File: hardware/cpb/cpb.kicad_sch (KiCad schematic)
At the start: 192 parts, among them J1 SW1, J10 RBFJUMP, J11 μSW2, J12 ADC15IN, J13 μSW3, J14 Conn_02x20_Odd_Even, J15 Conn_02x20_Odd_Even, J16 DAC1BUF, J17 DAC2BUF, J2 SW2, J3 SW3, J4 SW4, J5 ADC4IN, J6 PISW1, J7 ADC5IN, J8 ADC14IN, J9 μSW1, Q1 IRF7406, Q10 NPN, Q11 IRF7406, Q12 NPN, Q13 BSS138PS,115, Q14 BSS138PS,115, Q15 IRF7406, Q16 NPN, Q17 MBT2222ADW1T1, Q18 MBT2222ADW1T1, Q19 BSS138PS,115, Q2 IRF7406, Q20 BSS138PS,115, Q21 IRF7406, Q22 NPN, Q23 IRF7406, Q24 NPN, Q25 NPN, Q26 IRF7406, Q27 NPN, Q28 NPN, Q3 NPN, Q4 NPN, Q5 IRF7406, Q6 NPN, Q7 IRF7406, Q8 MBT2222ADW1T1, Q9 MBT2222ADW1T1, U1 KF33BDT, U2 AP63205WU, U3 SC16IS750xBS, U4 STM32L072R_B-Z_Tx, U5 TS912, U6 ADR420ARMZ, Y1 1.8432MHz

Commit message: cpb: add additional input/output channels
Adding more I/O to make the board more versatile.  While we're at
it, clean up schematic and make some early footprint/part number
assignments.  I like this board.
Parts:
- removed Q10, Q12, Q16, Q22, Q24, Q25, Q27, Q28, Q3, Q4, Q6: NPN, symbol Simulation_SPICE:NPN
- removed Q11, Q15, Q2, Q21, Q23, Q26, Q5, Q7: IRF7406, Package_SO:SOIC-8_3.9x4.9mm_P1.27mm, symbol Transistor_FET:IRF7404
- added D6: RED, LED_SMD:LED_0805_2012Metric, symbol Device:LED
- added Q11, Q2, Q5, Q7: IRF7306, Package_SO:SOIC-8_3.9x4.9mm_P1.27mm, symbol Transistor_FET:IRF7324
- added Q12, Q22, Q27, Q28, Q6: MBT2222ADW1T1, Package_TO_SOT_SMD:SOT-363_SC-70-6, symbol Transistor_BJT:MBT2222ADW1T1
- added Q4: PMBT2222A, Package_TO_SOT_SMD:SOT-23, symbol Transistor_BJT:PMBT2222A
- added R94: 1.5k, Resistor_SMD:R_0603_1608Metric, symbol Device:R
- C1, C11, C16, C17, C18, C19, C2, C20, C21, C22, C23, C24, C25, C26, C27, C28, C29, C3, C30, C31, C32, C33, C34, C35, C36, C4, C5, C6, C7, C8: footprint (none) -> Capacitor_SMD:C_0603_1608Metric
- C10, C12, C13, C14, C15, C9: LCSC C1589 -> (none); Manufacturer_Name Samsung Electro-Mechanics -> (none); Manufacturer_Part_Number CL10B103KB8NNNC -> (none)
- D1, D2, D3, D4, D5: value LED -> RED; footprint (none) -> LED_SMD:LED_0805_2012Metric; LCSC (none) -> C84256
- FB1: value FerriteBead -> BLM21BD272SN1L; footprint (none) -> Inductor_SMD:L_0805_2012Metric; LCSC (none) -> C85839
- H1, H2, H3, H4: DNI DNI -> (none)
- J14: DNI NP_JLC -> (none)
- L1: value 4.7u -> 4.7uH; footprint (none) -> Inductor_SMD:L_Vishay_IHLP-2020; LCSC (none) -> C844991
- Q1: LCSC (none) -> C3279781
- Q13, Q14, Q19, Q20: Flight BSS138PS,115 -> (none); Manufacturer_Part_Number BSS138PS,115 -> (none); Proto BSS138PS,115 -> (none)
- Q17, Q18, Q8, Q9: Flight MBT2222ADW1T1G -> (none); Manufacturer_Name onsemi -> (none); Manufacturer_Part_Number MBT2222ADW1T1G -> (none); Proto MBT2222ADW1T1G -> (none)
- R1, R10, R11, R12, R13, R14, R15, R16, R17, R18, R19, R2, R20, R21, R22, R23, R24, R25, R26, R27, R28, R29, R3, R30, R31, R32, R33, R34, R35, R36, R37, R38, R39, R4, R40, R41, R42, R43, R44, R45, R46, R47, R48, R49, R5, R50, R51, R52, R53, R54, R55, R56, R57, R58, R59, R6, R60, R61, R62, R63, R64, R65, R66, R67, R68, R69, R7, R70, R71, R72, R73, R74, R75, R76, R77, R78, R79, R8, R80, R81, R82, R83, R84, R85, R86, R87, R88, R89, R9, R90, R91, R92, R93: footprint (none) -> Resistor_SMD:R_0603_1608Metric
- U1: LCSC (none) -> C283274
- U2: LCSC (none) -> C2071056
- U3: LCSC (none) -> C2651891
- U4: LCSC (none) -> C915968
- U5: LCSC (none) -> C73655
- U6: LCSC (none) -> C208143
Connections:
- net +7.5V: now also Q11.1 (S1), Q11.3 (S2), Q2.1 (S1), Q2.3 (S2), Q5.1 (S1), Q5.3 (S2), Q7.1 (S1), Q7.3 (S2)
- net GND: now also D6.1 (K), Q12.1 (E1), Q12.4 (E2), Q22.1 (E1), Q22.4 (E2), Q27.1 (E1), Q27.4 (E2), Q28.1 (E1), Q28.4 (E2), Q4.2 (E), Q6.1 (E1), Q6.4 (E2)
- net MICRONRST: now also Q28.3 (C2)
- net PI3V3: now also R94.1
- net uSW1: now also U4.55 (PB3); no longer U4.42 (PA9)
- net uSW2: now also U4.56 (PB4); no longer U4.43 (PA10)
- net uSW3: now also U4.57 (PB5); no longer U4.44 (PA11)
- net at R22.2, R27.1: now also Q12.5 (B2)
- net at R23.2: now also Q12.3 (C2), Q5.4 (G2)
- net at R15.2, R19.1: now also Q12.2 (B1)
- net at J6.1 (Pin_1): now also Q7.7 (D1), Q7.8 (D1)
- net at R36.2, R39.1: now also Q22.2 (B1)
- net at R38.2: now also Q22.6 (C1), Q7.2 (G1)
- net at R18.2: now also Q12.6 (C1), Q5.2 (G1)
- net at R7.2: now also Q2.2 (G1), Q6.6 (C1)
- net at J1.1 (Pin_1): now also Q2.7 (D1), Q2.8 (D1)
- net at R71.2, R75.1: now also Q27.5 (B2)
- net at R4.2, R8.1: now also Q6.2 (B1)
- net at R3.2, R5.1: now also Q4.1 (B)
- net at R70.2, R76.1: now also Q28.5 (B2), Q28.6 (C1)
- net at J3.1 (Pin_1): now also Q5.7 (D1), Q5.8 (D1)
- net at R74.2: now also Q11.4 (G2), Q27.3 (C2)
- net at J9.1 (Pin_1): now also Q7.5 (D2), Q7.6 (D2)
- net at J13.1 (Pin_1): now also Q11.5 (D2), Q11.6 (D2)
- net at R56.2, R60.1: now also Q22.5 (B2)
- net at J4.1 (Pin_1): now also Q5.5 (D2), Q5.6 (D2)
- net at R10.2, R12.1: now also Q6.5 (B2)
- net at R11.2: now also Q2.4 (G2), Q6.3 (C2)
- net at R66.2: now also Q11.2 (G1), Q27.6 (C1)
- net at R64.2, R67.1: now also Q27.2 (B1)
- net at Q1.4 (G), R6.2: now also Q4.3 (C)
- net at R59.2: now also Q22.3 (C2), Q7.4 (G2)
- net at J15.12 (Pin_12), R72.2: now also Q28.2 (B1)
- net at J2.1 (Pin_1): now also Q2.5 (D2), Q2.6 (D2)
- net at J11.1 (Pin_1): now also Q11.7 (D1), Q11.8 (D1)
- net ADC4 renamed ADC6
- net ADC5 renamed ADC7
- new net: D6.2 (A), R94.2
- no-connect marks 45 -> 46
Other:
- note added: "Assuming 1.8Vf"
- note added: "Layout allows divider, control of impedance, LPF or AC coupling. All these inputs are also hooked to timer pins, so they can be used for capture or signal generation instead."
- note removed: "Layout allows divider, control of impedance, LPF or AC coupling."
- moved on the sheet: C12, C13, C14, C15, C28, C29, C32, C33, C34, C35, C36, FB1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

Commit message: cpb: add README, assign components, cleanup schematic
Lots of general cleanup and preparation to enter real assignment of
components and design review phase.
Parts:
- added Q3: PMBT2222A, Package_TO_SOT_SMD:SOT-23, symbol Transistor_BJT:PMBT2222A
- added R95: 10k, Resistor_SMD:R_0603_1608Metric, symbol Device:R
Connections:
- net +3.3V: now also R95.1
- net GND: now also Q3.2 (E)
- net MICRONRST: now also Q3.3 (C)
- net at U3.18 (GPIO5/~{DTR}): now also R9.2; no longer R9.1
- net GPIORST: now reaches U3.19 (GPIO6/~{CD})
- net GPIORST: now also Q3.1 (B), R95.2
- net PIFAILSAFE: now reaches U3.20 (GPIO7/~{RI})
- net PIFAILSAFE: now also J15.7 (Pin_7)
- net at D1.1 (K): now also R9.1; no longer R9.2
- no-connect marks 46 -> 44
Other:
- note added: "All resistors 1% tol! All capacitors on batt/7.5V rated >= 25V All capacitors on other rails rated at least 10V"
- note added: "Allow either pi or I2C-UART to hold microcontroller in reset. Ensure PI02W cannot hold down micro's reset when unpowered, but preserve sense of signal so existing software works."
- note added: "Connections to screws can be open, closed, resistive or capacitive."
- note added: "Per STMicro Recommendation"
- note added: "μController reset control"
- note removed: "All resistors 1% tol!"
- note removed: "Ensure PI02W cannot hold down micro's reset when unpowered."
- moved on the sheet: C1, C11, C12, C13, C14, C15, C6, C7, C8, D1, J12, J5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

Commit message: cpb: fix net name typos, assign footprints
Fix errors found by DRC.

Assign footprints so that it is possible to go to layout.

Select crystal for UART.
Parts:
- C10: value 22pF -> 15pF
- C9: value 33pF -> 22pF
- J10: footprint (none) -> Connector_PinHeader_2.54mm:PinHeader_1x02_P2.54mm_Horizontal
- J11, J12, J13, J2, J3, J4, J5, J6, J7, J8, J9: footprint (none) -> Connector_JST:JST_XH_B2B-XH-AM_1x02_P2.50mm_Vertical
- J15: footprint (none) -> Connector_PinHeader_2.54mm:PinHeader_2x20_P2.54mm_Vertical
- J16, J17: footprint (none) -> Connector_JST:JST_XH_B3B-XH-AM_1x03_P2.50mm_Vertical
- J77: renamed from J1; footprint (none) -> Connector_JST:JST_XH_B2B-XH-AM_1x02_P2.50mm_Vertical
- U5: footprint (none) -> Package_SO:SOIC-8_3.9x4.9mm_P1.27mm
- Y1: value 1.8432MHz -> 14.7456MHz; footprint (none) -> Crystal:Crystal_SMD_3225-4Pin_3.2x2.5mm; symbol Device:Crystal -> Device:Crystal_GND24_Small
- renumbered J14 to J1
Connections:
- net 3.3V is gone; now on net +3.3V: R13.1, R14.1, R16.1, R17.1, R24.1, R25.1, R34.1, R35.1, R40.1, R41.1, R49.1, R50.1
- net MICRORX is gone; now on net UCRX: J15.3 (Pin_3)
- net MICROTX is gone; now on net UCTX: J15.5 (Pin_5)
- net GND: now also Y1.2, Y1.4
- net at C10.1, U3.2 (XTAL1): now also Y1.3; no longer Y1.2
- no-connect marks 44 -> 60
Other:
- moved on the sheet: C27, R87, R88, U5B

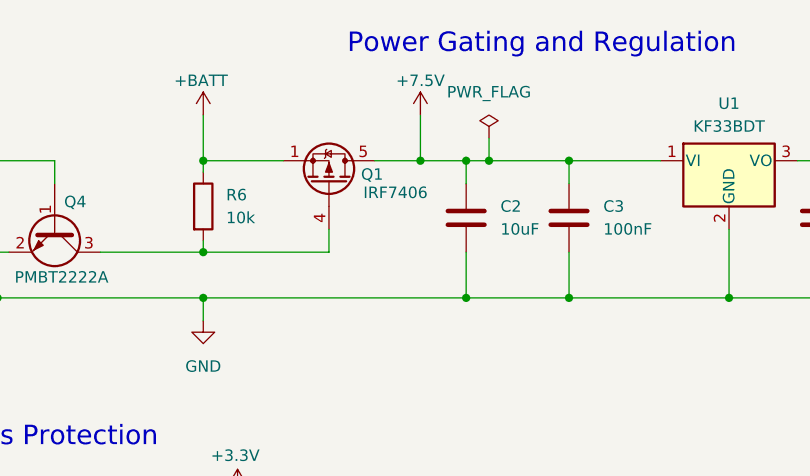
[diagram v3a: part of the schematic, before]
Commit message: cpb: substitute IRF9393 for IRF7406
IRF7406 availability is difficult right now, and IRF9393 seems to be
a strictly superior part.
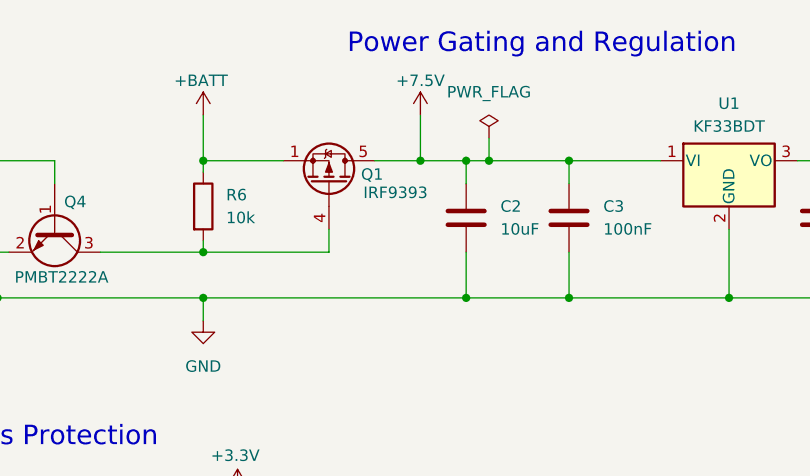
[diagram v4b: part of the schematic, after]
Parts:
- Q1: value IRF7406 -> IRF9393; LCSC C3279781 -> C520642
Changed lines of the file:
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@@
 			)
 		)
-		(property "Value" "IRF7406"
+		(property "Value" "IRF9393"
 			(at 88.9 32.766 90)
 			(effects
@@
 			)
 		)
-		(property "LCSC" "C3279781 "
+		(property "LCSC" "C520642"
 			(at 85.09 31.75 0)
 			(effects

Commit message: cpb: add octal H bridge, refactor to hierarchy
Big refactors here.

- Use hierarchical pages to represent duplicated circuits (e.g.
I2C protection, power switches).
- Add an octal H-bridge driver for magnetorquers
- Do some things for area reduction (resistor arrays)
- Attempt to name nets better and more consistently
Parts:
- removed C12, C13, C14, C15: 10nF, Capacitor_SMD:C_0603_1608Metric, symbol Device:C
- removed D1, D2: RED, LED_SMD:LED_0805_2012Metric, symbol Device:LED
- removed J2: SW2, Connector_JST:JST_XH_B2B-XH-AM_1x02_P2.50mm_Vertical, symbol Connector_Generic:Conn_01x02
- removed J3: SW3, Connector_JST:JST_XH_B2B-XH-AM_1x02_P2.50mm_Vertical, symbol Connector_Generic:Conn_01x02
- removed J4: SW4, Connector_JST:JST_XH_B2B-XH-AM_1x02_P2.50mm_Vertical, symbol Connector_Generic:Conn_01x02
- removed J5: ADC4IN, Connector_JST:JST_XH_B2B-XH-AM_1x02_P2.50mm_Vertical, symbol Connector_Generic:Conn_01x02
- removed J6: PISW1, Connector_JST:JST_XH_B2B-XH-AM_1x02_P2.50mm_Vertical, symbol Connector_Generic:Conn_01x02
- removed J7: ADC5IN, Connector_JST:JST_XH_B2B-XH-AM_1x02_P2.50mm_Vertical, symbol Connector_Generic:Conn_01x02
- removed J77: SW1, Connector_JST:JST_XH_B2B-XH-AM_1x02_P2.50mm_Vertical, symbol Connector_Generic:Conn_01x02
- removed J8: ADC14IN, Connector_JST:JST_XH_B2B-XH-AM_1x02_P2.50mm_Vertical, symbol Connector_Generic:Conn_01x02
- removed J9: μSW1, Connector_JST:JST_XH_B2B-XH-AM_1x02_P2.50mm_Vertical, symbol Connector_Generic:Conn_01x02
- removed Q11, Q2, Q5, Q7: IRF7306, Package_SO:SOIC-8_3.9x4.9mm_P1.27mm, symbol Transistor_FET:IRF7324
- removed Q12, Q17, Q18, Q22, Q27, Q6, Q8, Q9: MBT2222ADW1T1, Package_TO_SOT_SMD:SOT-363_SC-70-6, symbol Transistor_BJT:MBT2222ADW1T1
- removed Q13, Q14, Q19, Q20: BSS138PS,115, Package_TO_SOT_SMD:SOT-363_SC-70-6, symbol mainboard:BSS138DWQ-7
- removed Q3: PMBT2222A, Package_TO_SOT_SMD:SOT-23, symbol Transistor_BJT:PMBT2222A
- removed R1, R11, R13, R14, R16, R17, R18, R23, R34, R35, R38, R40, R41, R59, R6, R66, R7, R74, R95: 10k, Resistor_SMD:R_0603_1608Metric, symbol Device:R
- removed R10, R12, R15, R19, R22, R27, R3, R36, R39, R56, R60, R64, R67, R71, R75, R8: 4.7k, Resistor_SMD:R_0603_1608Metric, symbol Device:R
- removed R20, R21, R45, R46: 680, Resistor_SMD:R_0603_1608Metric, symbol Device:R
- removed R25, R49, R50: 100k, Resistor_SMD:R_0603_1608Metric, symbol Device:R
- removed R28, R29, R52, R53: 200k, Resistor_SMD:R_0603_1608Metric, symbol Device:R
- removed R32, R9, R94: 1.5k, Resistor_SMD:R_0603_1608Metric, symbol Device:R
- removed R68, R70, R72, R76: 3.3k, Resistor_SMD:R_0603_1608Metric, symbol Device:R
- added C3, C8: 22uF, Capacitor_SMD:C_0805_2012Metric, symbol Device:C
- added C5: 2.2uF, Capacitor_SMD:C_0603_1608Metric, symbol Device:C
- added D5: GPLED, LED_SMD:LED_0805_2012Metric, symbol Device:LED
- added D6: μCLED, LED_SMD:LED_0805_2012Metric, symbol Device:LED
- added D7: PILED, LED_SMD:LED_0805_2012Metric, symbol Device:LED
- added J10: SW1, Connector_JST:JST_PH_B2B-PH-K_1x02_P2.00mm_Vertical, symbol Connector_Generic:Conn_01x02
- added J14: μSW1, Connector_JST:JST_PH_B2B-PH-K_1x02_P2.00mm_Vertical, symbol Connector_Generic:Conn_01x02
- added J15: μSW2, Connector_JST:JST_PH_B2B-PH-K_1x02_P2.00mm_Vertical, symbol Connector_Generic:Conn_01x02
- added J16: μSW3, Connector_JST:JST_PH_B2B-PH-K_1x02_P2.00mm_Vertical, symbol Connector_Generic:Conn_01x02
- added J17: μSW4, Connector_JST:JST_PH_B2B-PH-K_1x02_P2.00mm_Vertical, symbol Connector_Generic:Conn_01x02
- added J2: I2CExt, Connector_JST:JST_PH_B5B-PH-K_1x05_P2.00mm_Vertical, symbol Connector_Generic:Conn_01x05
- added J7: ADC6/7, Connector_JST:JST_PH_B4B-PH-K_1x04_P2.00mm_Vertical, symbol Connector_Generic:Conn_01x04
- added J8: ADC2/3, Connector_JST:JST_PH_B4B-PH-K_1x04_P2.00mm_Vertical, symbol Connector_Generic:Conn_01x04
- added J9: 4FBRG, Connector_JST:JST_PHD_B8B-PHDSS_2x04_P2.00mm_Vertical, symbol Connector_Generic:Conn_01x08
- added Q4: PMBT2222A, Package_TO_SOT_SMD:SOT-23, symbol Transistor_BJT:PMBT2222A
- added R51: 10k, Resistor_SMD:R_0603_1608Metric, symbol Device:R
- added RN11: 3.3k, Resistor_SMD:R_Array_Convex_4x0603, symbol Device:R_Pack04_Split
- added RN12: 4.7k, Resistor_SMD:R_Array_Convex_4x0603, symbol Device:R_Pack04_Split
- added RN13: 1.5k, Resistor_SMD:R_Array_Convex_4x0603, symbol Device:R_Pack04_Split
- C10: renamed from C2; value 10uF -> 2.2uF
- D1: renamed from D3; value RED -> 7V5
- D2: renamed from D4; value RED -> 5V
- D3: renamed from D5; value RED -> 3V3
- D4: renamed from D6; value RED -> PI3V3
- J11: value μSW2 -> SW2; footprint Connector_JST:JST_XH_B2B-XH-AM_1x02_P2.50mm_Vertical -> Connector_JST:JST_PH_B2B-PH-K_1x02_P2.00mm_Vertical
- J12: value ADC15IN -> SW3; footprint Connector_JST:JST_XH_B2B-XH-AM_1x02_P2.50mm_Vertical -> Connector_JST:JST_PH_B2B-PH-K_1x02_P2.00mm_Vertical
- J13: value μSW3 -> PISW1; footprint Connector_JST:JST_XH_B2B-XH-AM_1x02_P2.50mm_Vertical -> Connector_JST:JST_PH_B2B-PH-K_1x02_P2.00mm_Vertical
- J3: renamed from J16; footprint Connector_JST:JST_XH_B3B-XH-AM_1x03_P2.50mm_Vertical -> Connector_JST:JST_PH_B3B-PH-K_1x03_P2.00mm_Vertical
- J4: renamed from J17; footprint Connector_JST:JST_XH_B3B-XH-AM_1x03_P2.50mm_Vertical -> Connector_JST:JST_PH_B3B-PH-K_1x03_P2.00mm_Vertical
- R24: value 100k -> 33
- R4: value 4.7k -> 200m 1W; footprint Resistor_SMD:R_0603_1608Metric -> Resistor_SMD:R_1206_3216Metric
- renumbered C20 to C1, C16 to C11, C23 to C12, C33 to C13, C3 to C14, C34 to C15, C35 to C16, C18 to C17, C24 to C18, C36 to C19, C21 to C2, C4 to C20, C5 to C21, C11 to C22, C30 to C23, C31 to C24, C17 to C26, C26 to C27, C6 to C28, C1 to C29, C28 to C30, C7 to C31, C29 to C32, C8 to C33, C9 to C34, C10 to C35, C22 to C4, C19 to C6, C27 to C7, C32 to C9, J15 to J1, J1 to J5, J10 to J99, Q4 to Q1, Q1 to Q2, Q28 to Q3, R84 to R10, R88 to R11, R77 to R12, R81 to R13, R83 to R14, R85 to R15, R89 to R16, R90 to R17, R62 to R18, R78 to R19, R86 to R20, R61 to R21, R43 to R22, R44 to R23, R91 to R25, R92 to R26, R26 to R27, R31 to R28, R33 to R29, R42 to R30, R93 to R31, R30 to R32, R37 to R33, R2 to R34, R82 to R37, R48 to R38, R58 to R39, R63 to R40, R69 to R41, R55 to R44, R65 to R45, R47 to R52, R51 to R53, R57 to R55, R79 to R6, R87 to R7, R73 to R8, R80 to R9, U5 to U1, U6 to U2, U1 to U3, U2 to U5, U3 to U6
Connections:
- net +3.3V: now also J2.2 (Pin_2), R51.1, RN11.5 (R4.2); no longer R24.1
- net +7.5V: now also C8.1, J2.3 (Pin_3)
- net +BATT: now also R4.1, C3.2, RN12.6 (R3.2); no longer Q2.1 (S), Q2.2 (S), Q2.3 (S)
- net ADC14: no longer R38.2, R39.1, R44.1
- net ADC15: no longer R40.2, R41.1, R45.1
- net ADC6: no longer U4.22 (PA6)
- net ADC7: no longer U4.23 (PA7)
- net GND: now also J11.1 (Pin_1), J13.1 (Pin_1), C3.1, C5.2, C8.2, D5.1 (K), D6.1 (K), D7.1 (K), J10.1 (Pin_1), J14.1 (Pin_1), J15.2 (Pin_2), J16.2 (Pin_2), J17.2 (Pin_2), J2.1 (Pin_1), J7.1 (Pin_1), J7.3 (Pin_3), J8.1 (Pin_1), J8.3 (Pin_3), Q4.2 (E), RN11.6 (R3.2), RN12.2 (R2.1); no longer J11.2 (Pin_2), J13.2 (Pin_2)
- net PI3V3: now also RN11.7 (R2.2), RN11.8 (R1.2), RN13.8 (R1.2)
- net REF2V: now also R24.2
- net SW1: no longer R4.1
- net UCRX: no longer R23.1, U4.59 (PB7)
- net UCTX: no longer R22.1, U4.58 (PB6)
- net at R32.2: now also J7.4 (Pin_4)
- net at R45.2: now also J8.2 (Pin_2); no longer J12.1 (Pin_1)
- net ADC2: now reaches U4.16 (PA2)
- net ADC2: now also R38.2, R39.1, R44.1
- net ADC3: now reaches U4.17 (PA3)
- net ADC3: now also R40.2, R41.1, R45.1
- net uSW4: now reaches U4.34 (PB13)
- net TIM3_CH2: now reaches U4.38 (PC7)
- net TIM3_CH2: now also RN13.6 (R3.2)
- net GPLED: now reaches U6.18 (GPIO5/~{DTR})
- net GPLED: now also RN13.7 (R2.2)
- net at R4.2: now also Q2.1 (S), Q2.2 (S), Q2.3 (S)
- net at Q1.1 (B): now also RN12.7 (R2.2), RN12.8 (R1.2); no longer R5.1
- net at D4.2 (A): now also RN13.1 (R1.1)
- net ~{RSTREQPI}: now reaches J1.12 (Pin_12), Q3.2 (B1)
- net ~{RSTREQPI}: now also RN11.1 (R1.1)
- net at Q3.5 (B2), Q3.6 (C1): now also RN11.2 (R2.1), RN11.3 (R3.1)
- net at R44.2: now also J8.4 (Pin_4)
- net at Q2.4 (G): now also C5.1, RN12.5 (R4.2); no longer Q1.3 (C)
- net at R33.2: now also J7.2 (Pin_2)
- net FBRGPWREN: now reaches J5.23 (Pin_23)
- net PILED: now reaches J1.33 (Pin_33)
- net PILED: now also RN13.5 (R4.2)
- net EN5V# renamed EN5V
- net EN5V: now also R5.1
- net GPIORST renamed RSTREQGPIO
- net RSTREQGPIO: now also Q4.1 (B), R51.2
- net MICRONRST renamed ~{MICRORST}
- net ~{MICRORST}: now also Q4.3 (C), RN11.4 (R4.1)
- net PICTS# renamed nPICTS
- net nPICTS: no longer J1.36 (Pin_36)
- net PIRTS# renamed nPIRTS
- net nPIRTS: no longer J1.11 (Pin_11)
- net PWRGATE renamed PRIPWREN
- net PRIPWREN: now also RN12.1 (R1.1)
- net RBF# renamed ~{RBF}
- net SCLMICRO renamed uSCL
- net SDAMICRO renamed uSDA
- new net: R24.1, U4.22 (PA6)
- new net: Q1.3 (C), RN12.3 (R3.1), RN12.4 (R4.1)
- new net: D5.2 (A), RN13.2 (R2.1)
- new net: D6.2 (A), RN13.3 (R3.1)
- new net: D7.2 (A), RN13.4 (R4.1)
- new net FourFullBridges/OUT1A: J9.1 (Pin_1)
- new net FourFullBridges/OUT1B: J9.2 (Pin_2)
- new net FourFullBridges/OUT2A: J9.3 (Pin_3)
- new net FourFullBridges/OUT2B: J9.4 (Pin_4)
- new net FourFullBridges/OUT3A: J9.5 (Pin_5)
- new net FourFullBridges/OUT3B: J9.6 (Pin_6)
- new net FourFullBridges/OUT4A: J9.7 (Pin_7)
- new net FourFullBridges/OUT4B: J9.8 (Pin_8)
- new net PairPowerSwitches1/OUT1: J10.2 (Pin_2)
- new net PairPowerSwitches1/OUT2: J11.2 (Pin_2)
- new net PairPowerSwitches2/OUT1: J12.1 (Pin_1)
- new net PairPowerSwitches2/OUT2: J13.2 (Pin_2)
- new net PairPowerSwitches3/OUT1: J14.2 (Pin_2)
- new net PairPowerSwitches3/OUT2: J15.1 (Pin_1)
- new net PairPowerSwitches4/OUT1: J16.1 (Pin_1)
- new net PairPowerSwitches4/OUT2: J17.1 (Pin_1)
- new net SCLEXT: J2.4 (Pin_4)
- new net SDAEXT: J2.5 (Pin_5)
- new net uRX: R23.1, U4.59 (PB7)
- new net uTX: R22.1, U4.58 (PB6)
- new net ~{PICTS}: J1.36 (Pin_36)
- new net ~{PIRTS}: J1.11 (Pin_11)
- no-connect marks 60 -> 55
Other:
- added sheet FourFullBridges (FourFullBridges.kicad_sch)
- added sheet I2CProtectionExt (I2CProtection.kicad_sch)
- added sheet I2CProtectionMicro (I2CProtection.kicad_sch)
- added sheet I2CProtectionUART (I2CProtection.kicad_sch)
- added sheet PairPowerSwitches1 (PairPowerSwitches.kicad_sch)
- added sheet PairPowerSwitches2 (PairPowerSwitches.kicad_sch)
- added sheet PairPowerSwitches3 (PairPowerSwitches.kicad_sch)
- added sheet PairPowerSwitches4 (PairPowerSwitches.kicad_sch)
- note added: "Address: 1001 000X (0x90 or 0x48)"
- note added: "Allow either pi or I2C-UART to hold microcontroller in reset. Ensure PI02W cannot hold down micro's reset when unpowered, but preserve sense of signal so existing programming software works."
- note added: "Also EVENTOUT, TIM3_CH1, or TIM22_CH1"
- note added: "Also EVENTOUT, TIM3_CH2, or TIM22_CH2"
- note added: "Also TIM2_CH3, TIM21_CH1, or UART TX Or comparator input."
- note added: "Also TIM2_CH4, TIM21_CH2, or UART RX; Or comparator input."
- note added: "Bulk Power Switches for Payloads"
- note added: "Decouple stack 3V3 even though we don't use it."
- note added: "Full Bridge for Magnetorquers"
- note added: "Layout allows divider, control of impedance, LPF or AC coupling. These pins have alternate functions (like timers for signal gen)."
- note added: "Linearize power switch to limit inrush; limit fault currents."
- note added: "PB6/PB7 are also an I2C SCL/SDA."
- note added: "Power is switched separately from everything else, for flexibility and robustness."
- note added: "Rail expected between 7.4 and 8.5V"
- note added: "Status LEDs"
- note added: "Threshold ~3A/V; dv/dt through thresh 909uV/us dA/dt 2.7mA/us XXX recalc 370us to reach an ampere; capacitors reach 7.5V in this time"
- note removed: "All resistors 1% tol! All capacitors on batt/7.5V rated >= 25V All capacitors on other rails rated at least 10V"
- note removed: "Allow either pi or I2C-UART to hold microcontroller in reset. Ensure PI02W cannot hold down micro's reset when unpowered, but preserve sense of signal so existing software works."
- note removed: "Bulk Power Switch for Payloads Pi-GPIO Controlled"
- note removed: "Bulk Power Switch for Payloads μController Controlled"
- note removed: "Bulk Power Switches for Payloads I2C-GPIO Controlled"
- note removed: "Distributed bypassing for stacked 3V3 (even though we don't use stacked 3V3)."
- note removed: "Layout allows divider, control of impedance, LPF or AC coupling. All these inputs are also hooked to timer pins, so they can be used for capture or signal generation instead."
- note removed: "PB6/PB7 also are an I2C SCL/SDA."
- moved on the sheet: C10, C14, C25, C27, C6, C7, H1, H2, H3, H4, J99, Q1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

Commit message: cpb: correct problems detected by ERC
Mostly duplicate/misnamed reference identifiers.
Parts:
- removed R24: 33, Resistor_SMD:R_0603_1608Metric, symbol Device:R
- added R18: 33, Resistor_SMD:R_0603_1608Metric, symbol Device:R
- renumbered J5 to J1, J1 to J6, R4 to R1, R14 to R10, R15 to R11, R16 to R12, R17 to R13, R18 to R14, R19 to R15, R20 to R16, R21 to R17, R5 to R19, R6 to R2, R22 to R20, R23 to R21, R25 to R22, R26 to R23, R27 to R24, R28 to R25, R29 to R26, R30 to R27, R31 to R28, R32 to R29, R7 to R3, R33 to R30, R34 to R31, R37 to R32, R38 to R33, R39 to R34, R40 to R35, R41 to R36, R44 to R37, R45 to R38, R51 to R39, R8 to R4, R52 to R40, R53 to R41, R54 to R42, R55 to R43, R9 to R5, R10 to R6, R11 to R7, R12 to R8, R13 to R9, RN12 to RN1, RN13 to RN2, RN11 to RN3
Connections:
- net SCLEXT is gone; now on net EXTSCL: J2.4 (Pin_4)
- net SCLUART is gone; now on net UARTSCL: U6.9 (SCL/SCLK)
- net SDAEXT is gone; now on net EXTSDA: J2.5 (Pin_5)
- net SDAUART is gone; now on net UARTSDA: U6.10 (SDA)
- net UCRX is gone; now on net uTX: J6.3 (Pin_3)
- net UCTX is gone; now on net uRX: J6.5 (Pin_5)
- net nPICTS is gone; now on net ~{PICTS}: U6.21 (~{RTS})
- net nPIRTS is gone; now on net ~{PIRTS}: U6.22 (~{CTS})
- net ADC6: now also U4.22 (PA6)
- net ADC7: now also U4.23 (PA7)
- net REF2V: now also R18.1
- net at U4.11 (PC3): now also R18.2
- net ADC14: no longer names the net of U4.24 (PC4)
- net ADC15: no longer names the net of U4.25 (PC5)
- net SW4: no longer names the net of U6.17 (GPIO4/~{DSR})
- no-connect marks 55 -> 57
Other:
- sheet FourFullBridges ports: added RAWPWR; removed PWR
- moved on the sheet: C1, C2, C4, U1C, U2

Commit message: cpb: fix connectors and other small details
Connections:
- net GND: now also J12.1 (Pin_1), J15.1 (Pin_1), J16.1 (Pin_1), J17.1 (Pin_1); no longer J12.2 (Pin_2), J15.2 (Pin_2), J16.2 (Pin_2), J17.2 (Pin_2)
- net PairPowerSwitches2/OUT1: now also J12.2 (Pin_2); no longer J12.1 (Pin_1)
- net PairPowerSwitches3/OUT2: now also J15.2 (Pin_2); no longer J15.1 (Pin_1)
- net PairPowerSwitches4/OUT1: now also J16.2 (Pin_2); no longer J16.1 (Pin_1)
- net PairPowerSwitches4/OUT2: now also J17.2 (Pin_2); no longer J17.1 (Pin_1)
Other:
- note added: "Threshold ~3A/V; dv/dt through thresh 591uV/us dA/dt 1.8mA/us peaks at around 800mA"
- note removed: "Threshold ~3A/V; dv/dt through thresh 909uV/us dA/dt 2.7mA/us XXX recalc 370us to reach an ampere; capacitors reach 7.5V in this time"
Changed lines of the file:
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@@
 		)
 	)
-	(text "Threshold ~3A/V;\ndv/dt through thresh 909uV/us\ndA/dt 2.7mA/us XXX recalc\n370us to reach an ampere;\ncapacitors reach 7.5V in this time"
+	(text "Threshold ~3A/V;\ndv/dt through thresh 591uV/us\ndA/dt 1.8mA/us\npeaks at around 800mA"
 		(exclude_from_sim no)
 		(at 68.326 45.212 0)
@@
 	(symbol
 		(lib_id "Connector_Generic:Conn_01x02")
-		(at 410.21 146.05 0)
+		(at 410.21 148.59 0)
+		(mirror x)
 		(unit 1)
 		(exclude_from_sim no)
@@
 		(dnp no)
 		(property "Reference" "J15"
-			(at 411.988 146.558 0)
+			(at 411.988 148.082 0)
 			(effects
 				(font
@@
 		)
 		(property "Value" "μSW2"
-			(at 411.734 148.59 0)
+			(at 411.734 146.05 0)
 			(effects
 				(font
@@
 		)
 		(property "Footprint" "Connector_JST:JST_PH_B2B-PH-K_1x02_P2.00mm_Vertical"
-			(at 410.21 146.05 0)
+			(at 410.21 148.59 0)
 			(effects
 				(font
@@
 		)
 		(property "Datasheet" "~"
-			(at 410.21 146.05 0)
+			(at 410.21 148.59 0)
 			(effects
 				(font
@@
 		)
 		(property "Description" "Generic connector, single row, 01x02, script generated (kicad-library-utils/schlib/autogen/connector/)"
-			(at 410.21 146.05 0)
+			(at 410.21 148.59 0)
 			(effects
 				(font
@@
 	(symbol
 		(lib_id "Connector_Generic:Conn_01x02")
-		(at 410.21 157.48 0)
+		(at 410.21 160.02 0)
+		(mirror x)
 		(unit 1)
 		(exclude_from_sim no)
@@
 		(dnp no)
 		(property "Reference" "J16"
-			(at 411.988 157.988 0)
+			(at 411.988 159.512 0)
 			(effects
 				(font
@@
 		)
 		(property "Value" "μSW3"
-			(at 411.734 160.02 0)
+			(at 411.734 157.48 0)
 			(effects
 				(font
@@
 		)
 		(property "Footprint" "Connector_JST:JST_PH_B2B-PH-K_1x02_P2.00mm_Vertical"
-			(at 410.21 157.48 0)
+			(at 410.21 160.02 0)
 			(effects
 				(font
@@
 		)
 		(property "Datasheet" "~"
-			(at 410.21 157.48 0)
+			(at 410.21 160.02 0)
 			(effects
 				(font
@@
 		)
 		(property "Description" "Generic connector, single row, 01x02, script generated (kicad-library-utils/schlib/autogen/connector/)"
-			(at 410.21 157.48 0)
+			(at 410.21 160.02 0)
 			(effects
 				(font
@@
 	(symbol
 		(lib_id "Connector_Generic:Conn_01x02")
-		(at 410.21 110.49 0)
+		(at 410.21 113.03 0)
+		(mirror x)
 		(unit 1)
 		(exclude_from_sim no)
@@
 		(dnp no)
 		(property "Reference" "J12"
-			(at 411.988 110.998 0)
+			(at 411.988 112.522 0)
 			(effects
 				(font
@@
 		)
 		(property "Value" "SW3"
-			(at 411.734 113.03 0)
+			(at 411.734 110.49 0)
 			(effects
 				(font
@@
 		)
 		(property "Footprint" "Connector_JST:JST_PH_B2B-PH-K_1x02_P2.00mm_Vertical"
-			(at 410.21 110.49 0)
+			(at 410.21 113.03 0)
 			(effects
 				(font
@@
 		)
 		(property "Datasheet" "~"
-			(at 410.21 110.49 0)
+			(at 410.21 113.03 0)
 			(effects
 				(font
@@
 		)
 		(property "Description" "Generic connector, single row, 01x02, script generated (kicad-library-utils/schlib/autogen/connector/)"
-			(at 410.21 110.49 0)
+			(at 410.21 113.03 0)
 			(effects
 				(font
@@
 	(symbol
 		(lib_id "Connector_Generic:Conn_01x02")
-		(at 410.21 168.91 0)
+		(at 410.21 171.45 0)
+		(mirror x)
 		(unit 1)
 		(exclude_from_sim no)
@@
 		(dnp no)
 		(property "Reference" "J17"
-			(at 411.988 169.418 0)
+			(at 411.988 170.942 0)
 			(effects
 				(font
@@
 		)
 		(property "Value" "μSW4"
-			(at 411.734 171.45 0)
+			(at 411.734 168.91 0)
 			(effects
 				(font
@@
 		)
 		(property "Footprint" "Connector_JST:JST_PH_B2B-PH-K_1x02_P2.00mm_Vertical"
-			(at 410.21 168.91 0)
+			(at 410.21 171.45 0)
 			(effects
 				(font
@@
 		)
 		(property "Datasheet" "~"
-			(at 410.21 168.91 0)
+			(at 410.21 171.45 0)
 			(effects
 				(font
@@
 		)
 		(property "Description" "Generic connector, single row, 01x02, script generated (kicad-library-utils/schlib/autogen/connector/)"
-			(at 410.21 168.91 0)
+			(at 410.21 171.45 0)
 			(effects
 				(font
